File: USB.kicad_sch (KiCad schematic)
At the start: 30 parts, among them J1 USB_C_Receptacle_USB2.0_16P, U1 USBLC6-2SC6, U2 AP63203WU, U6 TPS25940LRVCR, U7 TUSB320LAIRWBR

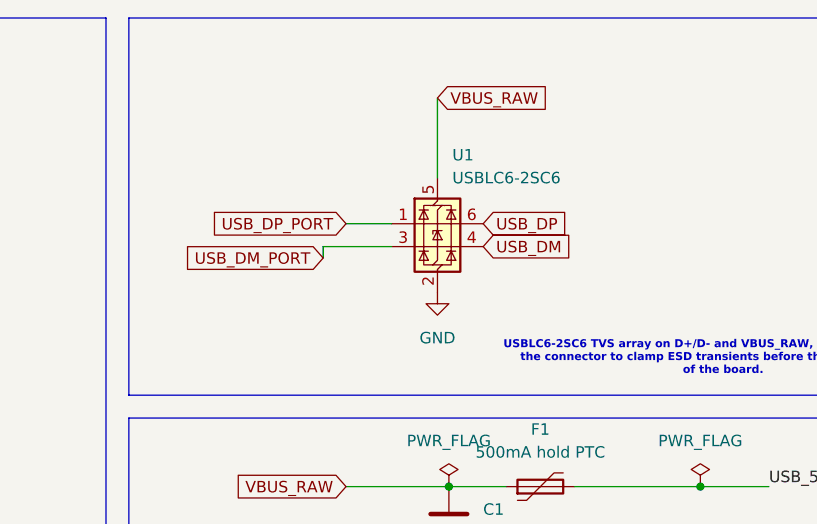
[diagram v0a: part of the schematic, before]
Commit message: Fixed usb routing
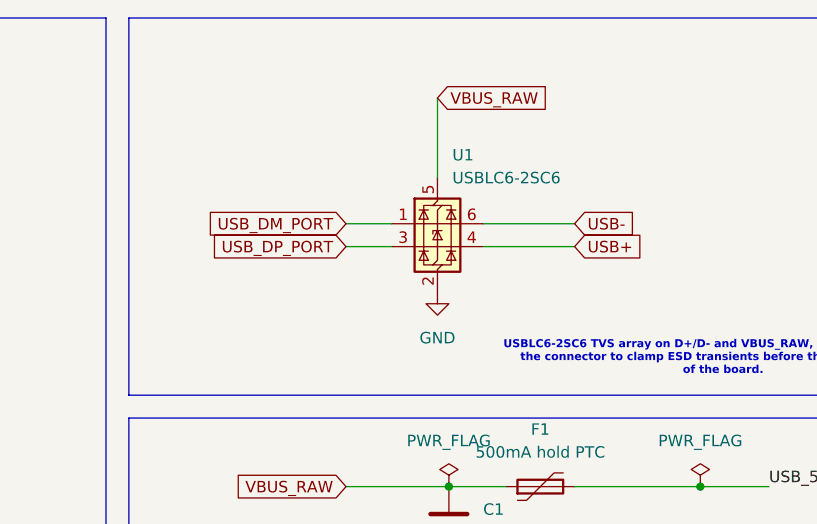
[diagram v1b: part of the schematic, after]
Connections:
- net USB_DM_PORT: now also U1.1 (I/O1); no longer U1.3 (I/O2)
- net USB_DP_PORT: now also U1.3 (I/O2); no longer U1.1 (I/O1)
- net USB_DM renamed USB+
- net USB_DP renamed USB-
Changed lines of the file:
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@@
 	(wire
 		(pts
-			(xy 111.76 39.37) (xy 119.38 39.37)
+			(xy 114.3 39.37) (xy 119.38 39.37)
 		)
 		(stroke
@@
 	(wire
 		(pts
+			(xy 129.54 36.83) (xy 139.7 36.83)
+		)
+		(stroke
+			(width 0)
+			(type default)
+		)
+	)
+	(wire
+		(pts
+			(xy 129.54 39.37) (xy 139.7 39.37)
+		)
+		(stroke
+			(width 0)
+			(type default)
+		)
+	)
+	(wire
+		(pts
 			(xy 297.18 147.32) (xy 297.18 148.59)
 		)
@@
 	(wire
 		(pts
-			(xy 111.76 39.37) (xy 111.76 40.64)
-		)
-		(stroke
-			(width 0)
-			(type default)
-		)
-	)
-	(wire
-		(pts
 			(xy 195.58 36.83) (xy 198.12 36.83)
 		)
@@
 		)
 	)
-	(global_label "USB_DM"
+	(global_label "USB-"
 		(shape input)
-		(at 129.54 39.37 0)
+		(at 139.7 36.83 0)
 		(fields_autoplaced yes)
 		(effects
@@
 		)
 		(property "Intersheetrefs" "${INTERSHEET_REFS}"
-			(at 140.0242 39.37 0)
+			(at 148.0676 36.83 0)
 			(hide yes)
 			(show_name no)
@@
 	(global_label "USB_DP_PORT"
 		(shape input)
-		(at 114.3 36.83 180)
+		(at 114.3 39.37 180)
 		(fields_autoplaced yes)
 		(effects
@@
 		)
 		(property "Intersheetrefs" "${INTERSHEET_REFS}"
-			(at 98.1915 36.83 0)
+			(at 98.1915 39.37 0)
 			(hide yes)
 			(show_name no)
@@
 		)
 	)
-	(global_label "USB_DP"
+	(global_label "USB+"
 		(shape input)
-		(at 129.54 36.83 0)
+		(at 139.7 39.37 0)
 		(fields_autoplaced yes)
 		(effects
@@
 		)
 		(property "Intersheetrefs" "${INTERSHEET_REFS}"
-			(at 139.8428 36.83 0)
+			(at 148.0676 39.37 0)
 			(hide yes)
 			(show_name no)
@@
 	(global_label "USB_DM_PORT"
 		(shape input)
-		(at 111.76 40.64 180)
+		(at 114.3 36.83 180)
 		(fields_autoplaced yes)
 		(effects
@@
 		)
 		(property "Intersheetrefs" "${INTERSHEET_REFS}"
-			(at 95.4701 40.64 0)
+			(at 98.0101 36.83 0)
 			(hide yes)
 			(show_name no)
@@
 		)
 	)
+	(embedded_fonts no)
 )
